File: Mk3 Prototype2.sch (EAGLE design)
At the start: 139 parts, among them IC1 TPD3E001DRL, IC2 TPS62082, IC3 STM32F401V, IC4 BQ2409X, IC40 MCP73831, IC6 CC3100MOD, IC7 BQ2970, J1 ZX62-AB-5PA(11), J2 ER-TFT024-3, J3 SWD_SHROUD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

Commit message: added some notes
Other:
- note added: "add i2c to edge connectors"
- note added: "connect i2c on pb11"
- note added: "speaker to tim1"
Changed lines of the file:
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@@
 <text x="-15.24" y="99.06" size="1.778" layer="91">JOY_RIGHT</text>
 <text x="-15.24" y="96.52" size="1.778" layer="91">JOY_CENTRE/BOOT0</text>
+<text x="-15.24" y="93.98" size="1.778" layer="91">connect i2c on pb11</text>
+<text x="-15.24" y="91.44" size="1.778" layer="91">speaker to tim1</text>
+<text x="-15.24" y="88.9" size="1.778" layer="91">add i2c to edge connectors</text>
 </plain>
 <instances>

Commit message: schamtic done
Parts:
- added R13, R9: 0603/??/5%, TiLDA Mk3 Parts:R-EU_0603K-SMALL
- added R24: 0/dnp, TiLDA Mk3 Parts:R-EU_0603K-SMALL
- R6: value 0603/2k/5% -> 0603/??/5%
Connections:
- removed net CHARGING: IC40.STAT, LED5.C
- removed net N$34: IC40.PROG, R6.1
- removed net N$58: IC6.UART1_TX, SV7.3
- removed net N$59: IC6.UART1_RX, SV7.2
- removed net N$8: IC3_PE.PE5
- removed net SPI3_NSS: IC3_PA.PA15, J2.CSX
- removed net USART3_RX: JP2.5
- new net FSMC_A23: IC3_PE.PE2, R24.2
- new net LCD_CS: IC3_PD.PD7, J2.CSX
- new net N$10: IC4.PRETERM, R6.1
- new net N$11: IC4.ISET, R9.1
- new net N$12: IC4.TS, R13.1
- new net N$9: IC4.!CHG, LED5.C
- new net USART1_RX: IC3_PB.PB7, IC6.UART1_TX, SV7.3
- new net USART1_TX: IC3_PB.PB6, IC6.UART1_RX, SV7.2
- net BOOT0: now also IC3_PE.PE0
- net BTN_MENU: now also IC3_PD.PD10
- net CC_RST: now also IC3_PC.PC3
- net GND: now also IC4.ISET2, IC4.VSS, R13.2, R9.2; no longer IC40.VSS
- net JOY_DWN: now also IC3_PD.PD6; no longer IC3_PD.PD12
- net JOY_LEFT: now also IC3_PA.PA15; no longer IC3_PD.PD11
- net JOY_RIGHT: now also IC3_PD.PD3
- net JOY_UP: now also IC3_PD.PD12; no longer IC3_PD.PD10
- net LCD_!RST: now also IC3_PE.PE1
- net LCD_MODE: now also IC3_PE.PE6
- net LCD_X: now also IC3_PE.PE4; no longer IC3_PC.PC3
- net LCD_Y: now also IC3_PE.PE5; no longer IC3_PC.PC13
- net MOM_DWN: now also IC3_PD.PD9
- net MOM_RIGHT: now also IC3_PD.PD8
- net SPI3_SCK: now also R24.1
- net TEAR: now also IC3_PE.PE3; no longer IC3_PD.PD3
- net USART6_RX: now also JP2.5
- net VBAT: now also IC4.OUT; no longer IC40.VBAT
- net VBUS: now also IC4.IN; no longer IC40.VIN
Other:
- note added: "/JOY_CENTRE"
- note added: "depends on whether battery has thermistor"
- note removed: "BTN_MENU"
- note removed: "CC_RST"
- note removed: "JOY_RIGHT"
- note removed: "MOM_DWN"
- note removed: "MOM_RIGHT"
- note removed: "lcd_mode"
- note removed: "lcd_rs"
- note removed: "lcdrst"
- note removed: "unconnected in parallel mode >"
- moved on the sheet: C3, IC4, IC40, LED5, R6

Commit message: load more routing
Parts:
- added R26: TEmp, TiLDA Mk3 Parts:R-EU_0603K-SMALL
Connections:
- new net N$8: IC3_PC.PC13, R26.1
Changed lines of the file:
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@@
 <part name="GND14" library="TiLDA Mk3 Parts" deviceset="GND" device=""/>
 <part name="R24" library="TiLDA Mk3 Parts" deviceset="R-EU_" device="0603K-SMALL" value="0/dnp"/>
+<part name="R26" library="TiLDA Mk3 Parts" deviceset="R-EU_" device="0603K-SMALL" value="TEmp"/>
 </parts>
 <sheets>
@@
 <instance part="GND14" gate="1" x="581.66" y="-20.32"/>
 <instance part="R24" gate="G$1" x="332.74" y="299.72" rot="R180"/>
+<instance part="R26" gate="G$1" x="40.64" y="99.06"/>
 </instances>
 <busses>
@@
 <pinref part="IC3" gate="_PD" pin="PD7"/>
 <wire x1="73.66" y1="116.84" x2="83.82" y2="116.84" width="0.1524" layer="91"/>
+<label x="76.2" y="116.84" size="1.778" layer="95"/>
 </segment>
 <segment>
@@
 </segment>
 </net>
+<net name="N$8" class="0">
+<segment>
+<pinref part="IC3" gate="_PC" pin="PC13"/>
+<pinref part="R26" gate="G$1" pin="1"/>
+<wire x1="33.02" y1="99.06" x2="35.56" y2="99.06" width="0.1524" layer="91"/>
+</segment>
+</net>

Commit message: load more routing
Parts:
- removed IC40: MCP73831, TiLDA Mk3 Parts:MCP73831
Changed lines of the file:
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@@
 <attribute name="FARNELL" value="1217769"/>
 </part>
-<part name="IC40" library="TiLDA Mk3 Parts" deviceset="MCP73831" device=""/>
 <part name="JP3" library="TiLDA Mk3 Parts" deviceset="M02" device="-JST-2MM-SMT">
 <attribute name="FARNELL" value="9492615"/>
@@
 <attribute name="FARNELL" x="337.82" y="109.22" size="1.778" layer="96" display="off"/>
 </instance>
-<instance part="IC40" gate="G$1" x="553.72" y="81.28"/>
 <instance part="JP3" gate="G$1" x="650.24" y="-27.94" rot="MR0">
 <attribute name="FARNELL" x="650.24" y="-27.94" size="1.778" layer="96" rot="MR0" display="off"/>

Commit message: getting there...
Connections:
- removed net N$62: JP3.2, R51.2
- removed net USB_ID_: IC3_PA.PA10, SJ3.1
- new net N$13: C48.2, IC7.BAT, R51.1
- net USB_ID: now also IC3_PA.PA10, SJ3.1
- net VBAT: now also JP3.2, R51.2; no longer C48.2, IC7.BAT, R51.1
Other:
- note added: "needed?"
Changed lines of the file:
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@@
 <text x="579.12" y="-45.72" size="1.778" layer="91" rot="R90">depends on whether battery has thermistor</text>
 <text x="83.82" y="71.12" size="1.778" layer="91">/JOY_CENTRE</text>
+<text x="162.56" y="106.68" size="1.778" layer="91">needed?</text>
 </plain>
 <instances>
@@
 </segment>
 </net>
-<net name="USB_ID" class="0">
-<segment>
-<pinref part="J1" gate="G$1" pin="USBID"/>
-<label x="132.08" y="109.22" size="1.778" layer="95"/>
-<pinref part="SJ3" gate="G$1" pin="2"/>
-<wire x1="114.3" y1="121.92" x2="127" y2="121.92" width="0.1524" layer="91"/>
-<wire x1="127" y1="121.92" x2="127" y2="109.22" width="0.1524" layer="91"/>
-<wire x1="127" y1="109.22" x2="149.86" y2="109.22" width="0.1524" layer="91"/>
-<junction x="127" y="109.22"/>
-<wire x1="127" y1="109.22" x2="127" y2="93.98" width="0.1524" layer="91"/>
-<pinref part="IC1" gate="G$1" pin="IO3"/>
-<wire x1="127" y1="93.98" x2="134.62" y2="93.98" width="0.1524" layer="91"/>
-</segment>
-</net>
 <net name="N$4" class="0">
 <segment>
@@
 <wire x1="607.06" y1="50.8" x2="607.06" y2="58.42" width="0.1524" layer="91"/>
 <junction x="607.06" y="58.42"/>
-<pinref part="IC7" gate="G$1" pin="BAT"/>
-<pinref part="R51" gate="G$1" pin="1"/>
-<wire x1="629.92" y1="-22.86" x2="627.38" y2="-22.86" width="0.1524" layer="91"/>
-<pinref part="C48" gate="G$1" pin="2"/>
-<wire x1="629.92" y1="-35.56" x2="629.92" y2="-22.86" width="0.1524" layer="91"/>
-<wire x1="629.92" y1="-22.86" x2="629.92" y2="-15.24" width="0.1524" layer="91"/>
+<wire x1="629.92" y1="-20.32" x2="629.92" y2="-15.24" width="0.1524" layer="91"/>
 <wire x1="629.92" y1="-15.24" x2="601.98" y2="-15.24" width="0.1524" layer="91"/>
-<junction x="629.92" y="-22.86"/>
 <wire x1="601.98" y1="58.42" x2="601.98" y2="-15.24" width="0.1524" layer="91"/>
 <junction x="601.98" y="58.42"/>
@@
 <wire x1="584.2" y1="58.42" x2="596.9" y2="58.42" width="0.1524" layer="91"/>
 <junction x="596.9" y="58.42"/>
+<pinref part="JP3" gate="G$1" pin="2"/>
+<wire x1="642.62" y1="-25.4" x2="640.08" y2="-25.4" width="0.1524" layer="91"/>
+<wire x1="640.08" y1="-25.4" x2="640.08" y2="-22.86" width="0.1524" layer="91"/>
+<pinref part="R51" gate="G$1" pin="2"/>
+<wire x1="640.08" y1="-22.86" x2="640.08" y2="-20.32" width="0.1524" layer="91"/>
+<wire x1="640.08" y1="-20.32" x2="629.92" y2="-20.32" width="0.1524" layer="91"/>
+<junction x="640.08" y="-22.86"/>
 </segment>
 <segment>
@@
 <label x="35.56" y="93.98" size="1.778" layer="95"/>
 <pinref part="IC3" gate="_PC" pin="PC15/OSC32_OUT"/>
-</segment>
-</net>
-<net name="USB_ID_" class="0">
-<segment>
-<wire x1="30.48" y1="175.26" x2="33.02" y2="175.26" width="0.1524" layer="91"/>
-<pinref part="IC3" gate="_PA" pin="PA10"/>
-<label x="33.02" y="175.26" size="1.778" layer="95"/>
-</segment>
-<segment>
-<label x="170.18" y="109.22" size="1.778" layer="95"/>
-<wire x1="177.8" y1="109.22" x2="160.02" y2="109.22" width="0.1524" layer="91"/>
-<pinref part="SJ3" gate="G$1" pin="1"/>
 </segment>
 </net>
@@
 </segment>
 </net>
-<net name="N$62" class="0">
-<segment>
-<pinref part="JP3" gate="G$1" pin="2"/>
-<wire x1="642.62" y1="-25.4" x2="640.08" y2="-25.4" width="0.1524" layer="91"/>
-<wire x1="640.08" y1="-25.4" x2="640.08" y2="-22.86" width="0.1524" layer="91"/>
-<pinref part="R51" gate="G$1" pin="2"/>
-</segment>
-</net>
 <net name="N$63" class="0">
 <segment>
@@
 </segment>
 </net>
+<net name="N$13" class="0">
+<segment>
+<pinref part="IC7" gate="G$1" pin="BAT"/>
+<pinref part="R51" gate="G$1" pin="1"/>
+<wire x1="629.92" y1="-22.86" x2="627.38" y2="-22.86" width="0.1524" layer="91"/>
+<junction x="629.92" y="-22.86"/>
+<pinref part="C48" gate="G$1" pin="2"/>
+<wire x1="629.92" y1="-35.56" x2="629.92" y2="-22.86" width="0.1524" layer="91"/>
+</segment>
+</net>
+<net name="USB_ID" class="0">
+<segment>
+<label x="170.18" y="109.22" size="1.778" layer="95"/>
+<wire x1="177.8" y1="109.22" x2="160.02" y2="109.22" width="0.1524" layer="91"/>
+<pinref part="SJ3" gate="G$1" pin="1"/>
+<wire x1="160.02" y1="109.22" x2="160.02" y2="111.76" width="0.1524" layer="91"/>
+<pinref part="J1" gate="G$1" pin="USBID"/>
+<label x="132.08" y="109.22" size="1.778" layer="95"/>
+<pinref part="SJ3" gate="G$1" pin="2"/>
+<wire x1="114.3" y1="121.92" x2="127" y2="121.92" width="0.1524" layer="91"/>
+<wire x1="127" y1="121.92" x2="127" y2="109.22" width="0.1524" layer="91"/>
+<wire x1="127" y1="109.22" x2="149.86" y2="109.22" width="0.1524" layer="91"/>
+<junction x="127" y="109.22"/>
+<wire x1="127" y1="109.22" x2="127" y2="93.98" width="0.1524" layer="91"/>
+<pinref part="IC1" gate="G$1" pin="IO3"/>
+<wire x1="127" y1="93.98" x2="134.62" y2="93.98" width="0.1524" layer="91"/>
+<wire x1="160.02" y1="111.76" x2="149.86" y2="111.76" width="0.1524" layer="91"/>
+<wire x1="149.86" y1="111.76" x2="149.86" y2="109.22" width="0.1524" layer="91"/>
+</segment>
+<segment>
+<wire x1="30.48" y1="175.26" x2="33.02" y2="175.26" width="0.1524" layer="91"/>
+<pinref part="IC3" gate="_PA" pin="PA10"/>
+<label x="33.02" y="175.26" size="1.778" layer="95"/>
+</segment>
+</net>

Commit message: mostly done now
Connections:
- net SDIO_SW: now also IC3_PD.PD11; no longer IC3_PA.PA8
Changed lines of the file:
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@@
 </segment>
 <segment>
-<pinref part="IC3" gate="_PA" pin="PA8"/>
-<wire x1="30.48" y1="180.34" x2="33.02" y2="180.34" width="0.1524" layer="91"/>
-<label x="33.02" y="180.34" size="1.778" layer="95"/>
+<pinref part="IC3" gate="_PD" pin="PD11"/>
+<wire x1="73.66" y1="104.14" x2="83.82" y2="104.14" width="0.1524" layer="91"/>
+<label x="76.2" y="104.14" size="1.778" layer="95"/>
 </segment>
 </net>

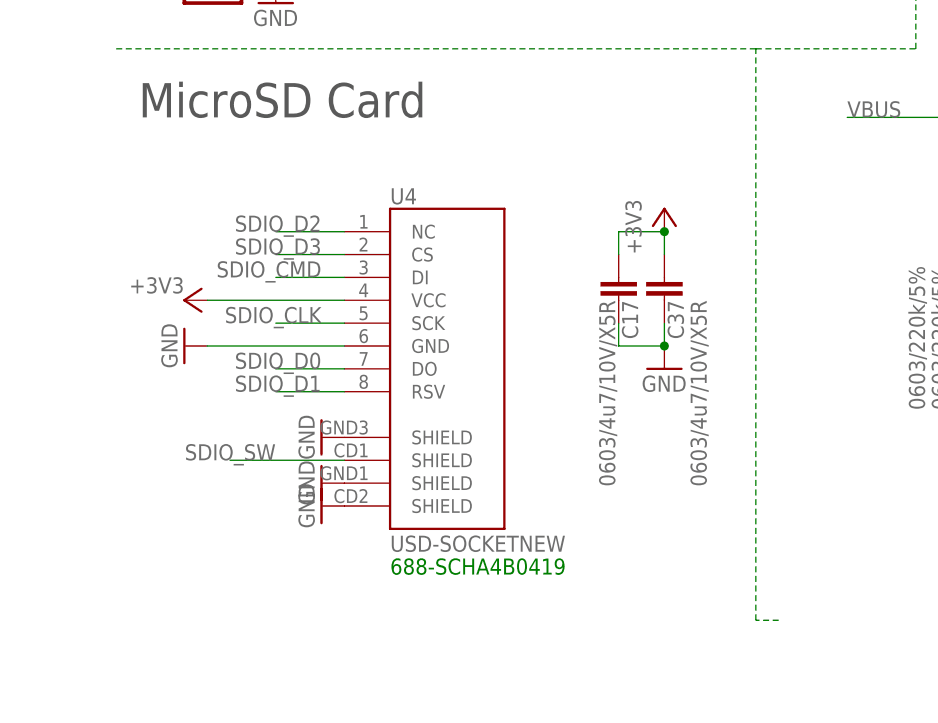
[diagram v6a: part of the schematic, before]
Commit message: changing usd holder
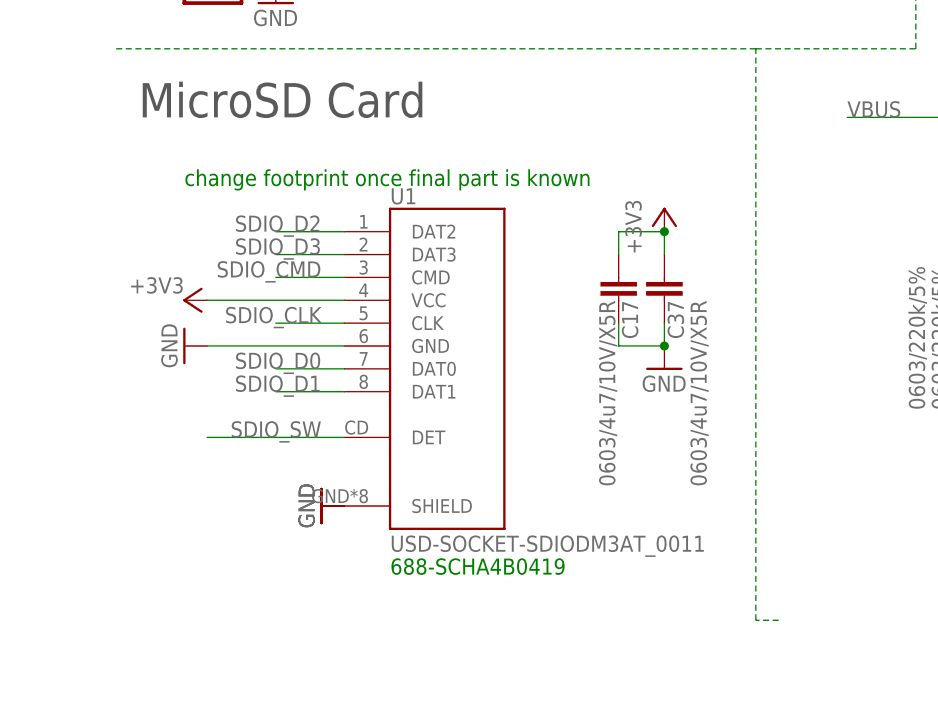
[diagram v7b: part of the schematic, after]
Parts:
- removed U4: USD-SOCKETNEW, TiLDA Mk3 Parts:USD-SOCKETNEW
- added U1: USD-SOCKET-SDIODM3AT_0011, TiLDA Mk3 Parts:USD-SOCKET-SDIODM3AT_0011
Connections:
- net +3V3: now also U1.VCC; no longer U4.VCC
- net GND: now also U1.GND, U1.SHIELD; no longer U4.GND, U4.SHIELD@1, U4.SHIELD@3, U4.SHIELD@4
- net SDIO_CLK: now also U1.CLK; no longer U4.SCK
- net SDIO_CMD: now also U1.CMD; no longer U4.DI
- net SDIO_D0: now also U1.DAT0; no longer U4.DO
- net SDIO_D1: now also U1.DAT1; no longer U4.RSV
- net SDIO_D2: now also U1.DAT2; no longer U4.NC
- net SDIO_D3: now also U1.DAT3; no longer U4.CS
- net SDIO_SW: now also U1.DET; no longer U4.SHIELD@2
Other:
- note added: "change footprint once final part is known"
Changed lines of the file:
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@@
 <?xml version="1.0" encoding="utf-8"?>
 <!DOCTYPE eagle SYSTEM "eagle.dtd">
-<eagle version="7.1.0">
+<eagle version="6.6.0">
 <drawing>
 <settings>
@@
 <part name="J3" library="dtb" deviceset="SWD_SHROUD" device="" value="SWD_SHROUD"/>
 <part name="GND46" library="TiLDA Mk3 Parts" deviceset="GND" device=""/>
-<part name="U4" library="TiLDA Mk3 Parts" deviceset="USD-SOCKET" device="NEW"/>
 <part name="+3V2" library="supply1" deviceset="+3V3" device=""/>
 <part name="+3V3" library="supply1" deviceset="+3V3" device=""/>
@@
 <part name="C17" library="TiLDA Mk3 Parts" deviceset="C-EU" device="C0603K-SMALL" value="0603/4u7/10V/X5R"/>
 <part name="GND67" library="TiLDA Mk3 Parts" deviceset="GND" device=""/>
-<part name="GND68" library="TiLDA Mk3 Parts" deviceset="GND" device=""/>
 <part name="GND69" library="TiLDA Mk3 Parts" deviceset="GND" device=""/>
 <part name="TP3" library="TiLDA Mk3 Parts" deviceset="TP" device="3.5MMEDGE" value="TP3.5MMEDGE"/>
@@
 <part name="R24" library="TiLDA Mk3 Parts" deviceset="R-EU_" device="0603K-SMALL" value="0/dnp"/>
 <part name="R26" library="TiLDA Mk3 Parts" deviceset="R-EU_" device="0603K-SMALL" value="TEmp"/>
+<part name="U1" library="TiLDA Mk3 Parts" deviceset="USD-SOCKET-SDIO" device="DM3AT_0011"/>
 </parts>
 <sheets>
@@
 <text x="83.82" y="71.12" size="1.778" layer="91">/JOY_CENTRE</text>
 <text x="162.56" y="106.68" size="1.778" layer="91">needed?</text>
+<text x="414.02" y="50.8" size="1.778" layer="91">change footprint once final part is known</text>
 </plain>
 <instances>
@@
 <instance part="J3" gate="G$1" x="27.94" y="17.78"/>
 <instance part="GND46" gate="1" x="10.16" y="7.62"/>
-<instance part="U4" gate="G$1" x="439.42" y="33.02"/>
 <instance part="+3V2" gate="G$1" x="375.92" y="53.34" smashed="yes" rot="R270">
 <attribute name="VALUE" x="375.92" y="53.34" size="1.778" layer="96"/>
@@
 </instance>
 <instance part="GND67" gate="1" x="467.36" y="30.48"/>
-<instance part="GND68" gate="1" x="429.26" y="22.86" rot="R270"/>
-<instance part="GND69" gate="1" x="429.26" y="17.78" rot="R270"/>
+<instance part="GND69" gate="1" x="429.26" y="15.24" rot="R270"/>
 <instance part="TP3" gate="G$1" x="640.08" y="170.18" smashed="yes"/>
 <instance part="TP1" gate="G$1" x="617.22" y="170.18" smashed="yes"/>
@@
 <instance part="R24" gate="G$1" x="332.74" y="299.72" rot="R180"/>
 <instance part="R26" gate="G$1" x="40.64" y="99.06"/>
+<instance part="U1" gate="G$1" x="441.96" y="30.48"/>
 </instances>
 <busses>
@@
 </segment>
 <segment>
-<pinref part="U4" gate="G$1" pin="GND"/>
 <wire x1="431.8" y1="33.02" x2="416.56" y2="33.02" width="0.1524" layer="91"/>
 <pinref part="GND53" gate="1" pin="GND"/>
+<pinref part="U1" gate="G$1" pin="GND"/>
 </segment>
 <segment>
@@
 <pinref part="GND67" gate="1" pin="GND"/>
 <junction x="467.36" y="33.02"/>
-</segment>
-<segment>
-<pinref part="U4" gate="G$1" pin="SHIELD@1"/>
-<pinref part="GND68" gate="1" pin="GND"/>
-</segment>
-<segment>
-<pinref part="U4" gate="G$1" pin="SHIELD@3"/>
-<pinref part="GND69" gate="1" pin="GND"/>
 </segment>
 <segment>
@@
 </segment>
 <segment>
-<pinref part="U4" gate="G$1" pin="SHIELD@4"/>
 <pinref part="GND103" gate="1" pin="GND"/>
+<pinref part="U1" gate="G$1" pin="SHIELD"/>
+<pinref part="U1" gate="G$1" pin="SHIELD"/>
+<pinref part="GND69" gate="1" pin="GND"/>
 </segment>
 <segment>
@@
 <net name="SDIO_D2" class="0">
 <segment>
-<pinref part="U4" gate="G$1" pin="NC"/>
 <wire x1="431.8" y1="45.72" x2="424.18" y2="45.72" width="0.1524" layer="91"/>
 <label x="429.26" y="45.72" size="1.778" layer="95" rot="MR0"/>
+<pinref part="U1" gate="G$1" pin="DAT2"/>
 </segment>
 <segment>
@@
 <net name="SDIO_D3" class="0">
 <segment>
-<pinref part="U4" gate="G$1" pin="CS"/>
 <wire x1="431.8" y1="43.18" x2="424.18" y2="43.18" width="0.1524" layer="91"/>
 <label x="429.26" y="43.18" size="1.778" layer="95" rot="MR0"/>
+<pinref part="U1" gate="G$1" pin="DAT3"/>
 </segment>
 <segment>
@@
 <net name="SDIO_CMD" class="0">
 <segment>
-<pinref part="U4" gate="G$1" pin="DI"/>
 <wire x1="431.8" y1="40.64" x2="424.18" y2="40.64" width="0.1524" layer="91"/>
 <label x="429.26" y="40.64" size="1.778" layer="95" rot="MR0"/>
+<pinref part="U1" gate="G$1" pin="CMD"/>
 </segment>
 <segment>
@@
 <net name="SDIO_CLK" class="0">
 <segment>
-<pinref part="U4" gate="G$1" pin="SCK"/>
 <wire x1="431.8" y1="35.56" x2="424.18" y2="35.56" width="0.1524" layer="91"/>
 <label x="429.26" y="35.56" size="1.778" layer="95" rot="MR0"/>
+<pinref part="U1" gate="G$1" pin="CLK"/>
 </segment>
 <segment>
@@
 <net name="SDIO_D0" class="0">
 <segment>
-<pinref part="U4" gate="G$1" pin="DO"/>
 <wire x1="431.8" y1="30.48" x2="424.18" y2="30.48" width="0.1524" layer="91"/>
 <label x="429.26" y="30.48" size="1.778" layer="95" rot="MR0"/>
+<pinref part="U1" gate="G$1" pin="DAT0"/>
 </segment>
 <segment>
@@
 <net name="SDIO_D1" class="0">
 <segment>
-<pinref part="U4" gate="G$1" pin="RSV"/>
 <wire x1="431.8" y1="27.94" x2="424.18" y2="27.94" width="0.1524" layer="91"/>
 <label x="429.26" y="27.94" size="1.778" layer="95" rot="MR0"/>
+<pinref part="U1" gate="G$1" pin="DAT1"/>
 </segment>
 <segment>
@@
 </segment>
 <segment>
-<pinref part="U4" gate="G$1" pin="VCC"/>
 <wire x1="431.8" y1="38.1" x2="416.56" y2="38.1" width="0.1524" layer="91"/>
 <pinref part="+3V7" gate="G$1" pin="+3V3"/>
+<pinref part="U1" gate="G$1" pin="VCC"/>
 </segment>
 <segment>
@@
 <net name="SDIO_SW" class="0">
 <segment>
-<wire x1="419.1" y1="20.32" x2="431.8" y2="20.32" width="0.1524" layer="91"/>
-<label x="424.18" y="20.32" size="1.778" layer="95" rot="MR0"/>
-<pinref part="U4" gate="G$1" pin="SHIELD@2"/>
-</segment>
-<segment>
+<wire x1="416.56" y1="22.86" x2="431.8" y2="22.86" width="0.1524" layer="91"/>
+<label x="429.26" y="22.86" size="1.778" layer="95" rot="MR0"/>
+<pinref part="U1" gate="G$1" pin="DET"/>
+<pinref part="U1" gate="G$1" pin="DET"/>
+</segment>
+<segment>

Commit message: moving things around
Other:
- note added: "connect pin 10"
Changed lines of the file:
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@@
 <text x="162.56" y="106.68" size="1.778" layer="91">needed?</text>
 <text x="414.02" y="50.8" size="1.778" layer="91">change footprint once final part is known</text>
+<text x="693.42" y="160.02" size="1.778" layer="91">connect pin 10</text>
 </plain>
 <instances>
